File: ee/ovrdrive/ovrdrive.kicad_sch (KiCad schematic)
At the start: 47 parts, among them J2 USB3_A, J4 Micro_SD_Card_Det_Hirose_DM3AT, SW1 SW_Push, U1 CH569W, U2 TLV62569DBV, U3 TLV62569DBV, Y2 30Mhz

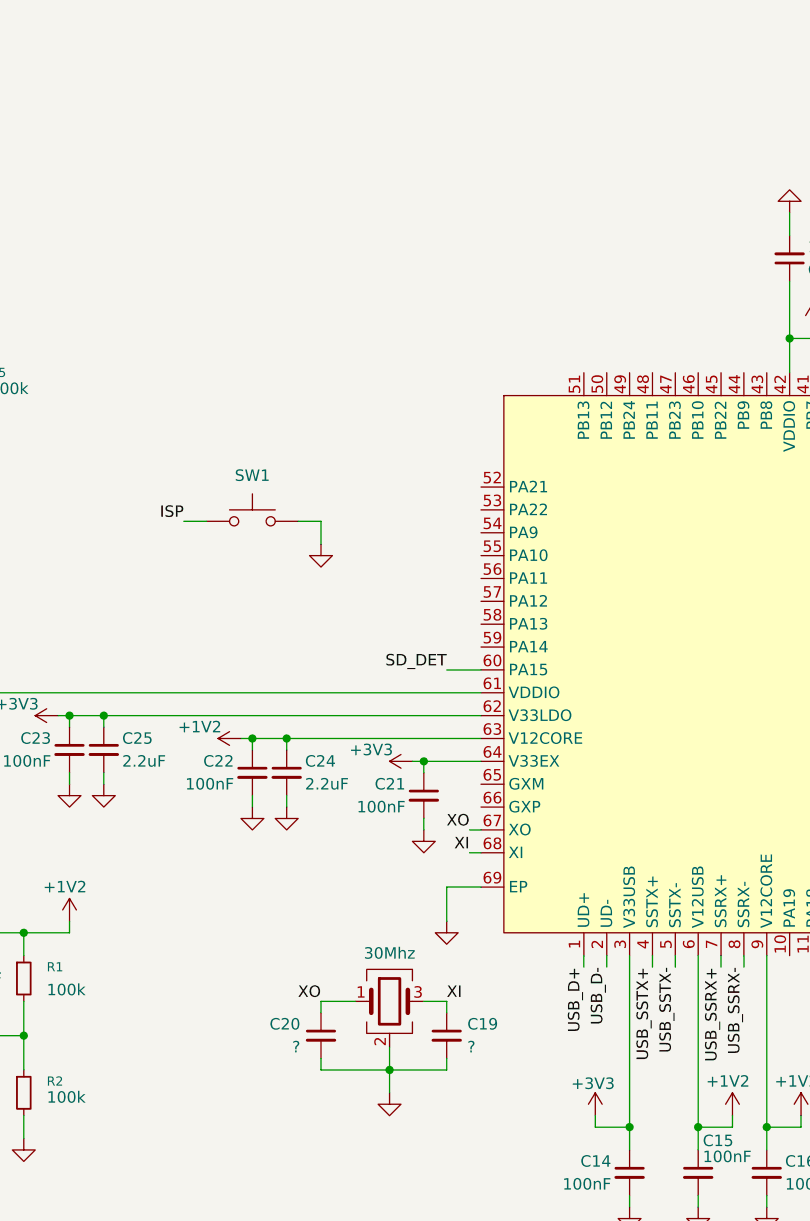
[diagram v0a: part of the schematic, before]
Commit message: Finished routing of PCB.
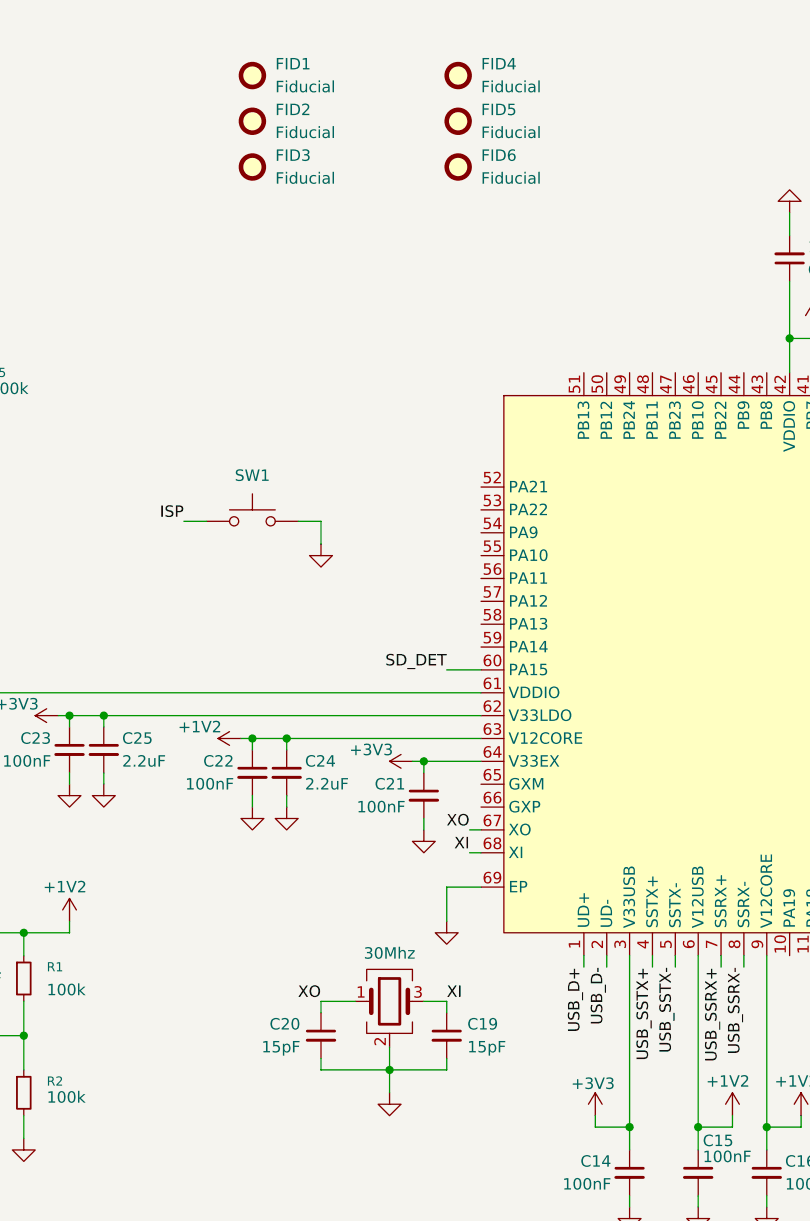
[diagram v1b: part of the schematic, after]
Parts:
- added FID1, FID2, FID3, FID4, FID5, FID6: Fiducial, Fiducial:Fiducial_0.5mm_Mask1mm, symbol Mechanical:Fiducial
- C1, C11, C12, C13, C2, C5, C6, C7, C9: MPN (none) -> CL05A226MQ5N6J8
- C10, C14, C15, C16, C17, C18, C21, C22, C23, C26, C27, C28, C3, C4, C8: MPN (none) -> CL05B104KP5NNNC
- C19, C20: value ? -> 15pF; MPN (none) -> CL05C150JB5NNNC
- C24, C25: MPN (none) -> CL05A225MQ5NNNC
- J2: MPN (none) -> 692112030100
- R1, R2, R4, R5: MPN (none) -> RC0402FR-07100KL
- R3: MPN (none) -> RC0402FR-07453KL
- TP1, TP2, TP3: MPN (none) -> DNP
- U1: MPN (none) -> CH569W
- U2, U3: MPN (none) -> TLV62569DBV

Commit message: Added release script
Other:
- company: Interrupt Labs -> Rootkit Labs
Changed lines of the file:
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@@
 		(date "2026-03-19")
 		(rev "R0.1")
-		(company "Interrupt Labs")
+		(company "Rootkit Labs")
 		(comment 1 "Ryan Walker")
 		(comment 2 "info@rootkitlabs.com")
